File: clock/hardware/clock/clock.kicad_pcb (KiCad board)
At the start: 2 copper layers, 45.7 x 58.4 mm, 27 parts, among them J1 USB_B_Micro, J2 7SEG_DEBUG, J3 Conn_ARM_JTAG_SWD_10, U1 LM1117-3.3, U2 AS1115, U3 LTC-4727JS, U4 STM32L151C8TxA, Y1 32.768kHz

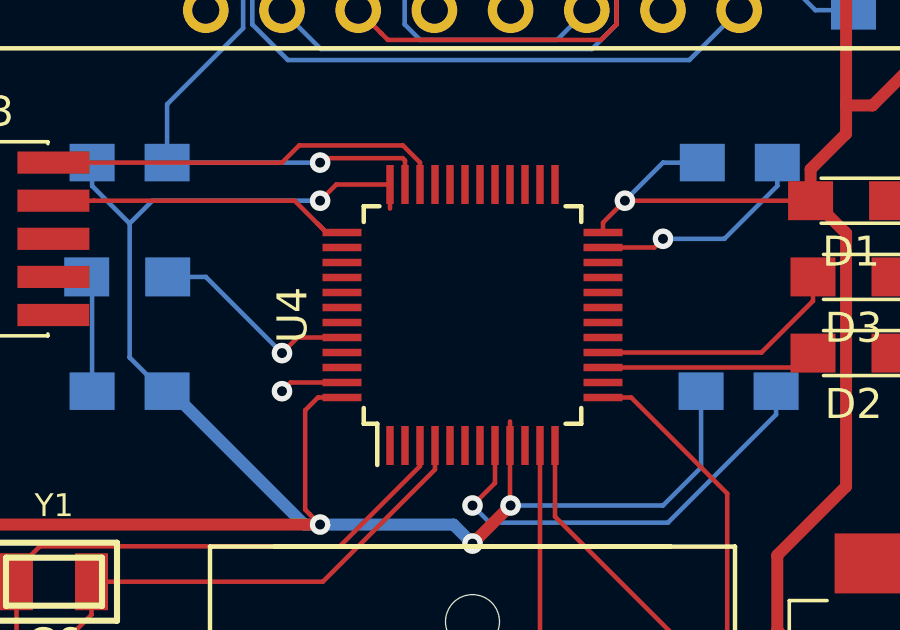
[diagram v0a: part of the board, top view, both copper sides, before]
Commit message: Remove stray tracks.
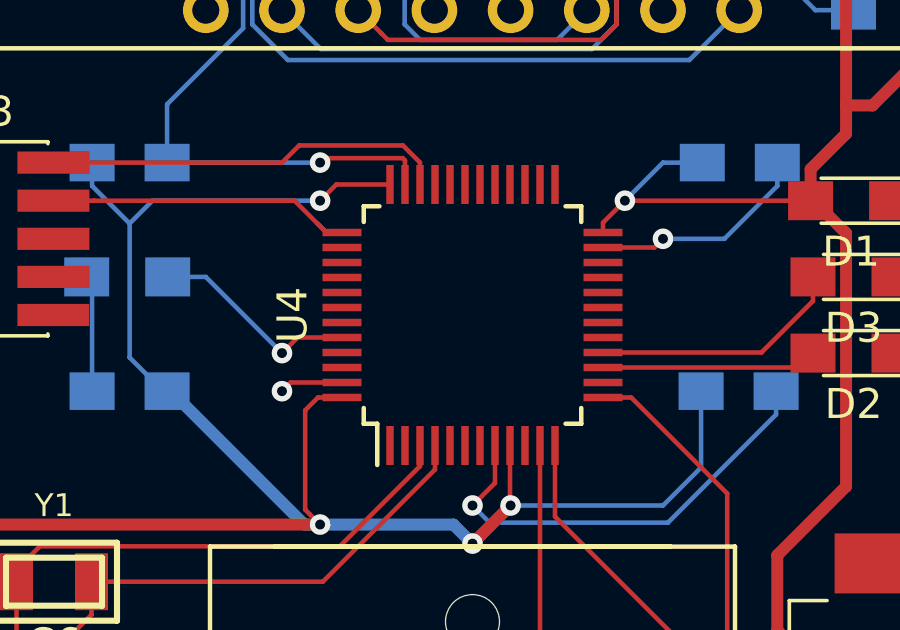
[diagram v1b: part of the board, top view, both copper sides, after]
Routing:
- net +3V3: track 201.0 -> 199.4 mm
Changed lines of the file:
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@@
     (thickness 1.6)
     (drawings 9)
-    (tracks 343)
+    (tracks 341)
     (zones 0)
     (modules 27)
@@
   (via (at 87.63 25.4) (size 0.6858) (drill 0.3302) (layers F.Cu B.Cu) (net 22))
   (segment (start 86.6775 29.0957) (end 86.6775 27.18359) (width 0.1524) (layer B.Cu) (net 22))
-  (segment (start 86.6775 27.18359) (end 86.639399 27.145489) (width 0.1524) (layer B.Cu) (net 22))
-  (segment (start 86.639399 27.145489) (end 86.639399 26.194511) (width 0.1524) (layer B.Cu) (net 22))
-  (segment (start 86.639399 26.194511) (end 87.43391 25.4) (width 0.1524) (layer B.Cu) (net 22))
   (segment (start 80.771999 37.591999) (end 80.01 36.83) (width 0.1524) (layer F.Cu) (net 22))
   (segment (start 81.000601 37.820601) (end 80.771999 37.591999) (width 0.1524) (layer F.Cu) (net 22))
@@
   (segment (start 85.07 51.34) (end 85.07 53.32) (width 0.1524) (layer F.Cu) (net 1))
   (segment (start 95.09 43.18) (end 88.9 43.18) (width 0.1524) (layer F.Cu) (net 1))
-  (segment (start 81.07 43.4424) (end 81.07 42.64) (width 0.1524) (layer F.Cu) (net 1))
-  (segment (start 85.07 50.5376) (end 85.07 51.34) (width 0.1524) (layer F.Cu) (net 1))
   (segment (start 73.515 49.53) (end 72.39 48.405) (width 0.1524) (layer B.Cu) (net 1))
   (segment (start 73.64 49.53) (end 73.515 49.53) (width 0.1524) (layer B.Cu) (net 1))
@@
   (segment (start 76.82 58.46) (end 83.86 58.46) (width 0.1524) (layer F.Cu) (net 20))
   (segment (start 89.11 49.74) (end 88.17 49.74) (width 0.1524) (layer F.Cu) (net 20))
+  (segment (start 86.6775 27.18359) (end 86.639399 27.145489) (width 0.1524) (layer B.Cu) (net 22))
+  (segment (start 86.639399 26.194511) (end 87.43391 25.4) (width 0.1524) (layer B.Cu) (net 22))
+  (segment (start 86.639399 27.145489) (end 86.639399 26.194511) (width 0.1524) (layer B.Cu) (net 22))
   (via (at 88.9 24.13) (size 0.6858) (drill 0.3302) (layers F.Cu B.Cu) (net 23))
   (segment (start 90.17 36.83) (end 91.160601 35.839399) (width 0.1524) (layer B.Cu) (net 23))

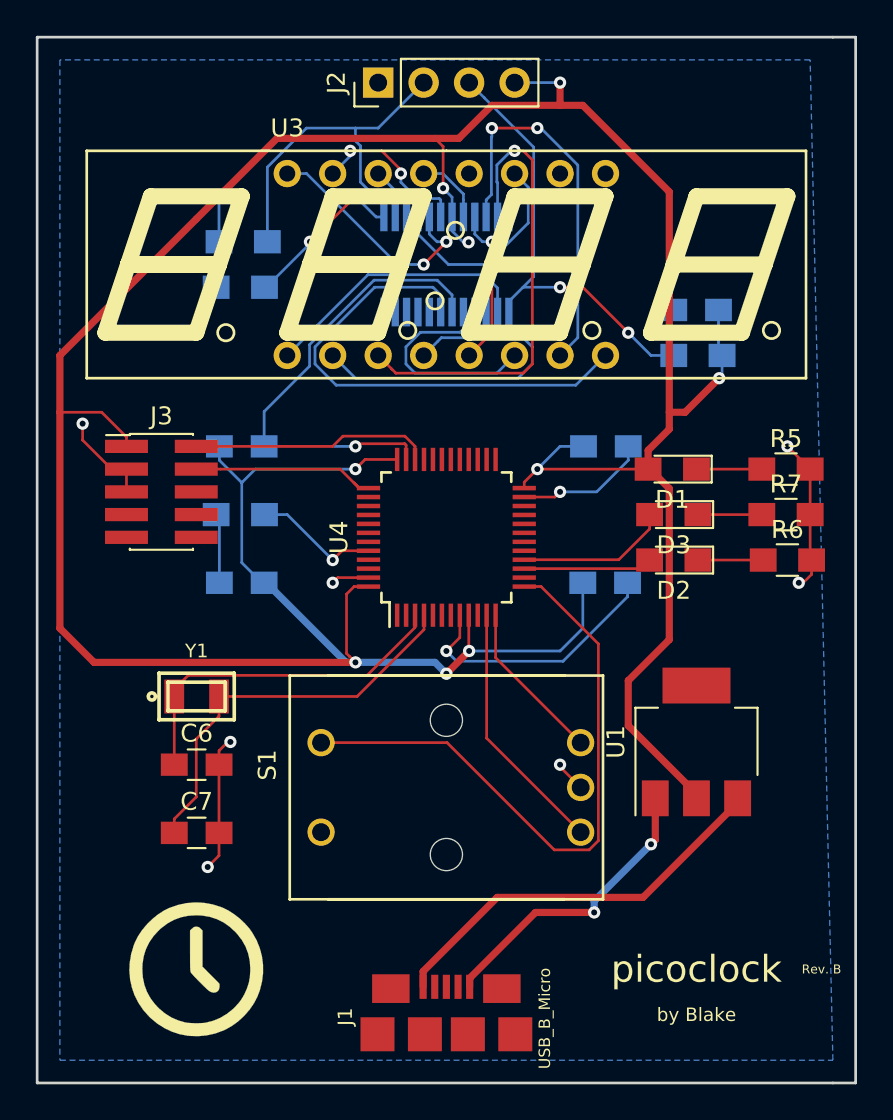
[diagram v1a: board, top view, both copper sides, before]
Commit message: Rev C: Wire in missing I2C bus. Reorder LEDs. Move power rail to avoid colliding with status LEDs.
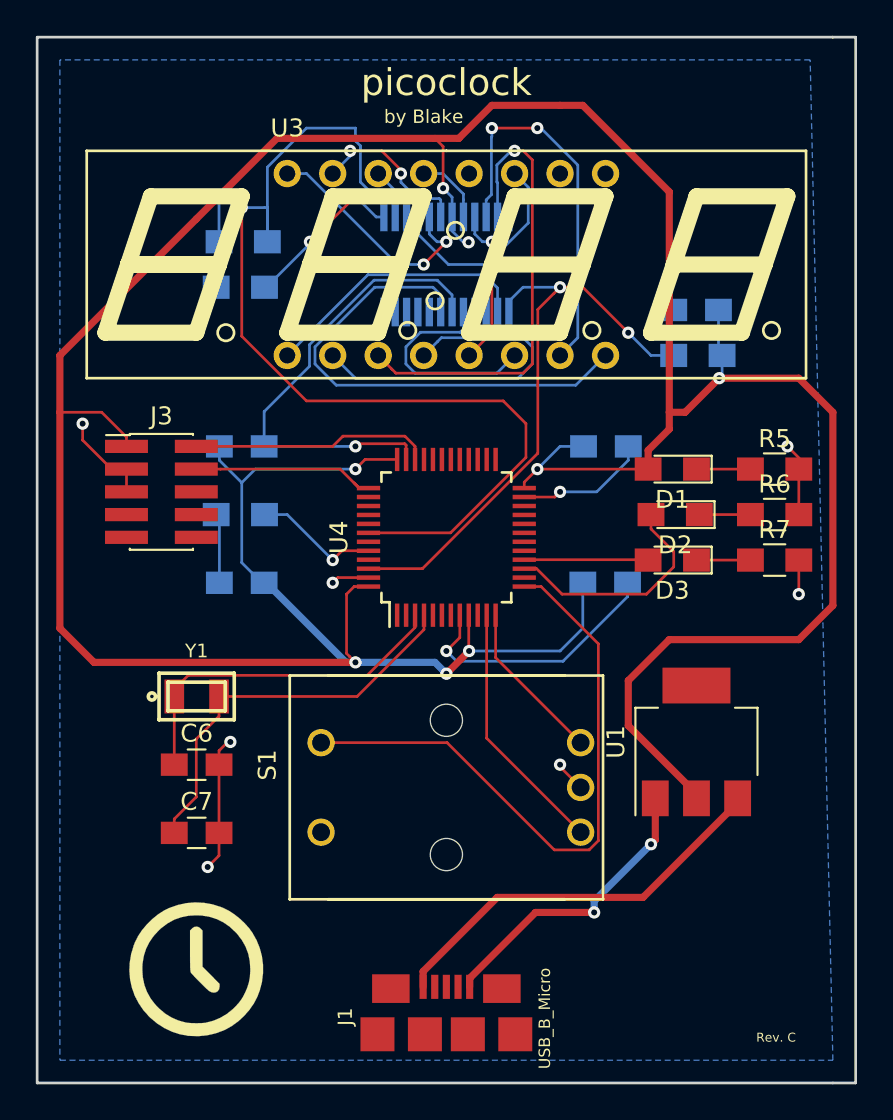
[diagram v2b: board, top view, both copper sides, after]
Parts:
- removed J2: 7SEG_DEBUG, Pin_Headers:Pin_Header_Straight_1x04_Pitch2.54mm
- moved R6 2.64 mm to (102.2, 45.7)
- moved R7 2.62 mm to (102.2, 48.3)
- moved D2 2.54 mm to (96.6, 45.7)
- moved D3 2.54 mm to (96.4, 48.3)
- moved R5 0.64 mm to (102.2, 43.2)
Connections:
- R1 pad 2: Net-(J2-Pad3) -> /7SEG_SDA
- R2 pad 2: Net-(J2-Pad2) -> /7SEG_SCL
- U2 pad 1: Net-(J2-Pad3) -> /7SEG_SDA
- U2 pad 14: Net-(J2-Pad2) -> /7SEG_SCL
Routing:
- net /7SEG_SCL: track 0.00 -> 57.4 mm, vias 0 -> 1
- net /7SEG_SDA: track 0.00 -> 33.6 mm, vias 0 -> 2
- net Net-(J2-Pad3): track 24.9 -> 0.00 mm, vias 2 -> 0
- net Net-(J2-Pad2): track 21.6 -> 0.00 mm
- net +3V3: track 199.4 -> 213.5 mm, vias 10 -> 9
- net /STATUS_OK: track 7.20 -> 13.0 mm
- net GND: track 95.9 -> 93.5 mm
- net /STATUS_ERR: track 8.51 -> 6.93 mm
- net Net-(D2-Pad1): track 3.65 -> 2.86 mm
- net Net-(D1-Pad1): track 3.65 -> 3.02 mm
- net Net-(D3-Pad1): track 3.57 -> 3.02 mm
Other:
- net class 3v: trace_width 0.1524 -> 0.4
- board text added: "Rev. C"
- board text removed: "Rev. B"

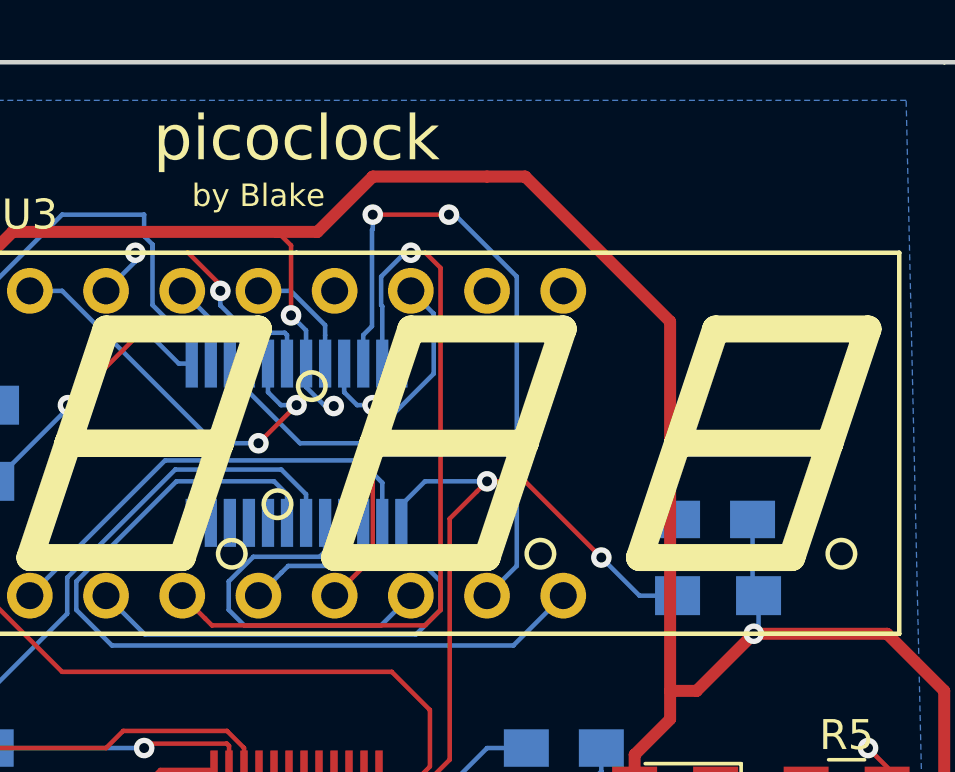
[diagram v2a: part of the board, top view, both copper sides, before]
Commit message: Move AS1115 decoupling cap.
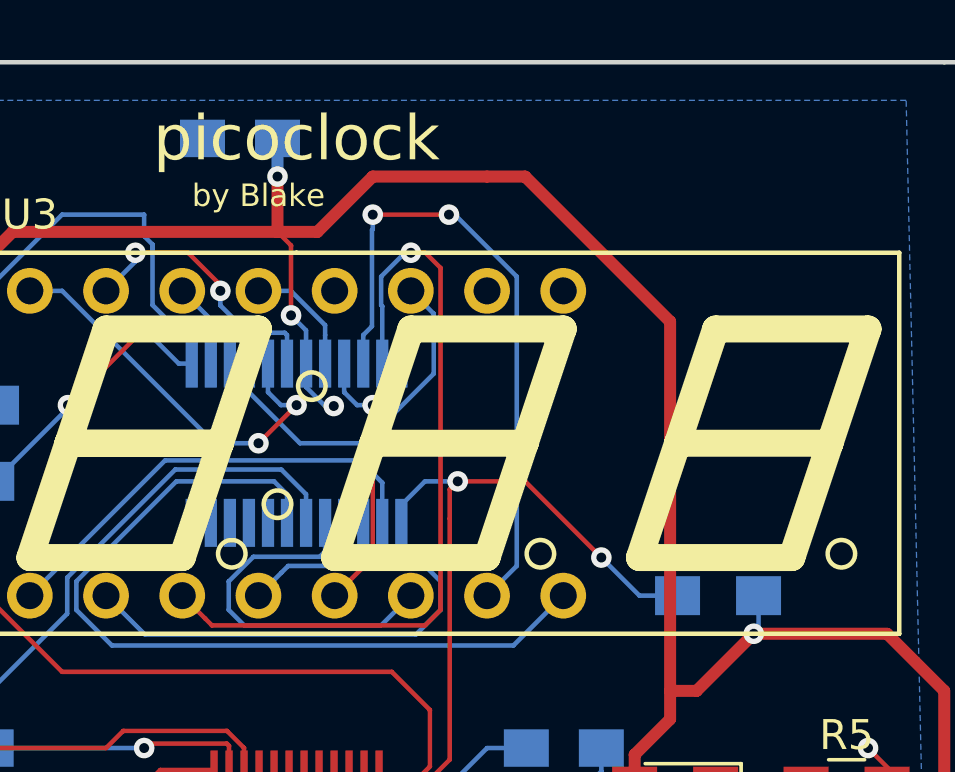
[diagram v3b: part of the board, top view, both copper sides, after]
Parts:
- moved C5 20.3 mm to (81.9, 21.6)
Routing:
- net +3V3: track 213.5 -> 214.3 mm, vias 9 -> 10
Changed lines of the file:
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@@
     (thickness 1.6)
     (drawings 9)
-    (tracks 352)
+    (tracks 354)
     (zones 0)
     (modules 26)
@@
   )
   (module Capacitors_SMD:C_0805_HandSoldering (layer B.Cu)
-    (at 97.77 34.29 180)
+    (at 81.935 21.59 180)
     (descr "Capacitor SMD 0805, hand soldering")
     (tags "capacitor 0805")
     (attr smd)
-    (fp_text reference C5 (at 0 1.75 180) (layer B.SilkS)
+    (fp_text reference C5 (at 3.83 0 180) (layer B.SilkS)
       (effects (font (size 1 1) (thickness 0.15)) (justify mirror))
     )
@@
   (segment (start 70.96 33.02) (end 70.96 30.64) (width 0.1524) (layer B.Cu) (net 1))
   (segment (start 99.02 36.63) (end 99.22 36.83) (width 0.1524) (layer B.Cu) (net 1))
-  (segment (start 99.02 34.29) (end 99.02 36.63) (width 0.1524) (layer B.Cu) (net 1))
   (via (at 99.06 38.1) (size 0.6858) (drill 0.3302) (layers F.Cu B.Cu) (net 1))
   (segment (start 99.22 37.94) (end 99.06 38.1) (width 0.1524) (layer B.Cu) (net 1))
@@
   (segment (start 93.98 54.997401) (end 96.272401 52.705) (width 0.4) (layer F.Cu) (net 1))
   (segment (start 93.98 57.51) (end 93.98 54.997401) (width 0.4) (layer F.Cu) (net 1))
+  (via (at 83.185 22.86) (size 0.6858) (drill 0.3302) (layers F.Cu B.Cu) (net 1))
+  (segment (start 83.185 21.59) (end 83.185 22.86) (width 0.4) (layer B.Cu) (net 1))
+  (segment (start 83.185 22.86) (end 83.185 24.704699) (width 0.4) (layer F.Cu) (net 1))
   (segment (start 76.174589 36.228255) (end 76.17459 37.431746) (width 0.1524) (layer B.Cu) (net 2))
   (segment (start 84.1375 34.4043) (end 84.1375 33.4519) (width 0.1524) (layer B.Cu) (net 2))
@@
   (segment (start 95.25 36.83) (end 93.98 35.56) (width 0.1524) (layer B.Cu) (net 47))
   (segment (start 96.52 36.83) (end 95.25 36.83) (width 0.1524) (layer B.Cu) (net 47))
-  (via (at 90.17 33.02) (size 0.6858) (drill 0.3302) (layers F.Cu B.Cu) (net 47))
-  (segment (start 91.44 33.02) (end 90.17 33.02) (width 0.1524) (layer F.Cu) (net 47))
-  (segment (start 93.98 35.56) (end 91.44 33.02) (width 0.1524) (layer F.Cu) (net 47))
-  (segment (start 90.17 33.02) (end 88.1018 33.02) (width 0.1524) (layer B.Cu) (net 47))
   (segment (start 87.3125 33.8093) (end 88.1018 33.02) (width 0.1524) (layer B.Cu) (net 47))
-  (segment (start 89.827101 33.362899) (end 90.17 33.02) (width 0.1524) (layer F.Cu) (net 47))
-  (segment (start 88.925411 34.264589) (end 89.827101 33.362899) (width 0.1524) (layer F.Cu) (net 47))
   (segment (start 88.925411 42.298107) (end 88.925411 34.264589) (width 0.1524) (layer F.Cu) (net 47))
   (segment (start 82.483518 48.74) (end 88.925411 42.298107) (width 0.1524) (layer F.Cu) (net 47))
   (segment (start 79.47 48.74) (end 82.483518 48.74) (width 0.1524) (layer F.Cu) (net 47))
+  (segment (start 88.925411 33.28669) (end 89.192101 33.02) (width 0.1524) (layer F.Cu) (net 47))
+  (via (at 89.192101 33.02) (size 0.6858) (drill 0.3302) (layers F.Cu B.Cu) (net 47))
+  (segment (start 88.925411 34.264589) (end 88.925411 33.28669) (width 0.1524) (layer F.Cu) (net 47))
+  (segment (start 89.192101 33.02) (end 88.1018 33.02) (width 0.1524) (layer B.Cu) (net 47))
+  (segment (start 91.44 33.02) (end 93.98 35.56) (width 0.1524) (layer F.Cu) (net 47))
+  (segment (start 89.192101 33.02) (end 91.44 33.02) (width 0.1524) (layer F.Cu) (net 47))
   (segment (start 73.82 26.31391) (end 76.00391 24.13) (width 0.1524) (layer B.Cu) (net 50))
   (segment (start 79.534511 27.660601) (end 80.479801 27.660601) (width 0.1524) (layer B.Cu) (net 50))
